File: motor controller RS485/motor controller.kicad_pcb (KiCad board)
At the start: 2 copper layers, 38 x 18 mm, 29 parts, among them IC1 MA702, IC2 MC33926PNB, IC3 LP38690SD-ADJ_NOPB, IC4 LTC2850IS8PBF, J1 Conn_01x04_Male, J2 Conn_01x04_Male, J3 Conn_01x04_Male, M1 Motor_DC, U1 STM32L432KCUx, Y1 32mhz

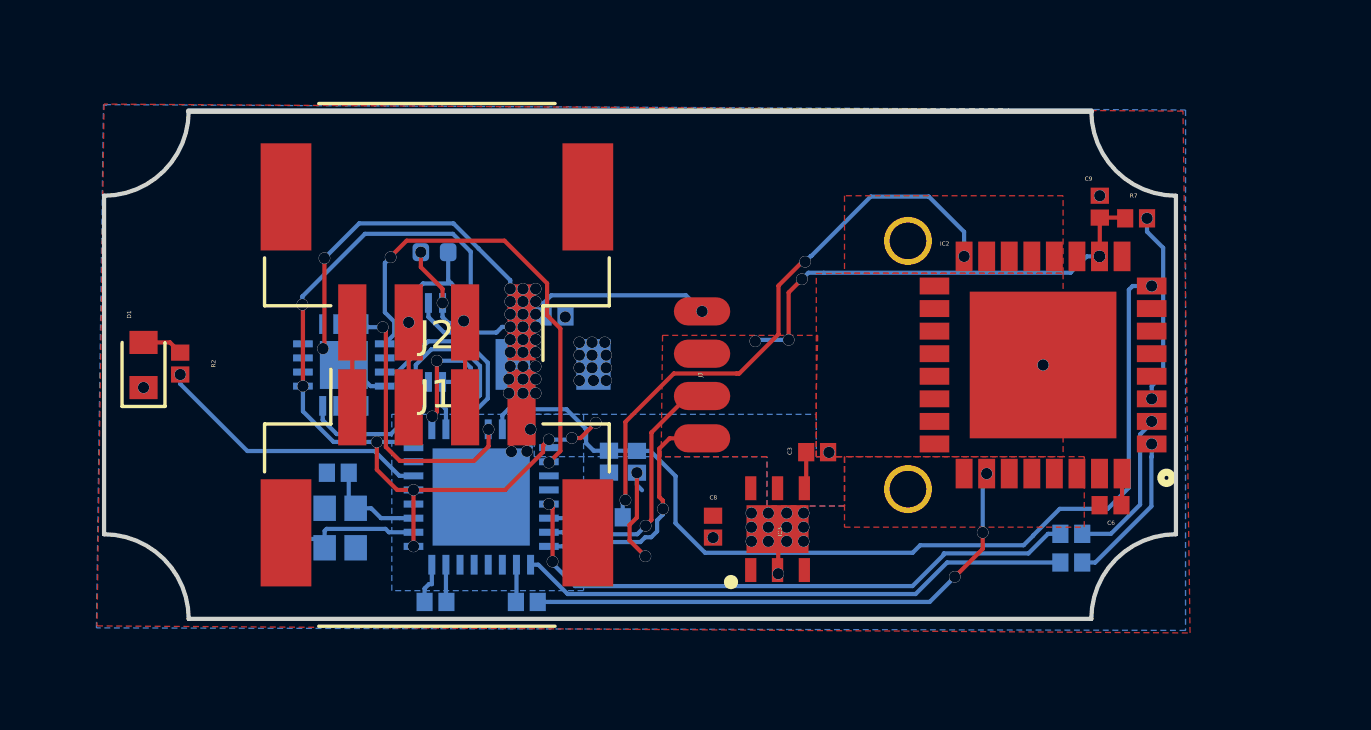
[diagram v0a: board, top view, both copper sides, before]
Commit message: Updated RS485 variant
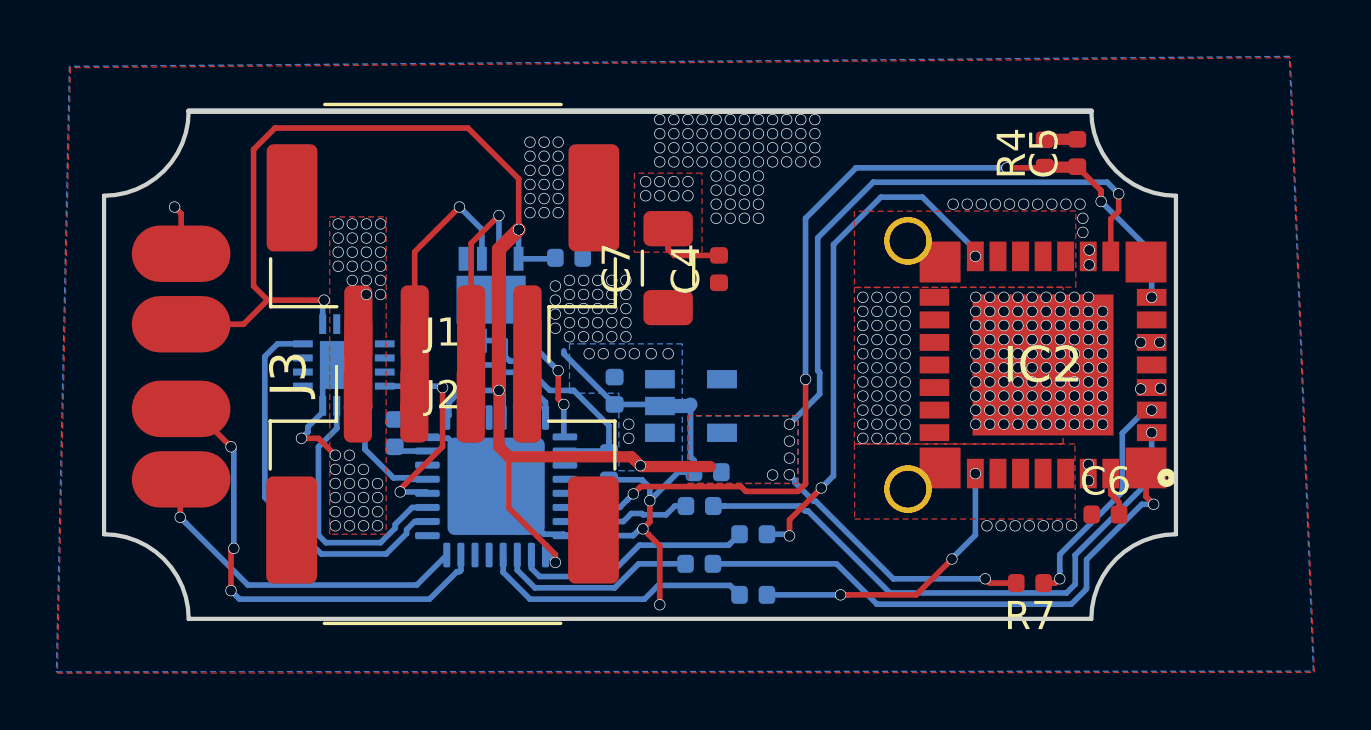
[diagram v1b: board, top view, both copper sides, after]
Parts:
- removed C8, C9: 1UF, Capacitor_SMD:C_0402_1005Metric
- removed D1: LED, LED_SMD:LED_0603_1608Metric
- removed IC4: LTC2850IS8PBF, SOIC127P600X175-8N
- removed R2: 330, Resistor_SMD:R_0402_1005Metric
- removed Y1: 32mhz, Crystal:Crystal_SMD_2016-4Pin_2.0x1.6mm
- added U2: MIC5504-3.3YM5, Package_TO_SOT_SMD:SOT-23-5, B.Cu at (20.8, 10.5)
- C1, C2: value 10pF -> C
- C3: moved to B.Cu
- C4, C5, C7, R4: moved to F.Cu
- IC2: footprint MC33926PNB:QFN80P800X800X220-33N -> MC33926:QFN80P800X800X220-33N
- IC3: value LP38690SD-ADJ_NOPB -> SN65HVD75DRBT; footprint LP38690SD-ADJ_NOPB:SON95P300X300X80-7N -> SN65HVD75DRBT:SON65P300X300X100-9N-D; moved to B.Cu
- R3: value 120 -> 10K
- moved C5 19.9 mm to (34.5, 1.49), turned to 90 degrees
- moved J3 18.5 mm to (2.73, 9.06)
- moved R4 18.1 mm to (33.4, 1.50), turned to 90 degrees
- moved R7 13.5 mm to (32.8, 16.7)
- moved R6 13.2 mm to (21.1, 14.0)
- moved R5 13.2 mm to (21.1, 16.1)
- moved IC3 13.0 mm to (13.7, 6.69)
- moved C1 12.6 mm to (18.1, 9.91)
- moved C2 11.2 mm to (16.5, 5.20), turned to 180 degrees
- moved R3 9.79 mm to (17.9, 12.6), turned to 90 degrees
- moved R8 8.03 mm to (23.0, 17.1)
- moved J2 7.98 mm to (12.0, 5.02), turned to 180 degrees
- moved J1 7.91 mm to (12.0, 12.9), turned to 0 degrees
- moved R1 6.16 mm to (10.3, 11.4), turned to 90 degrees
- moved C4 6.07 mm to (21.8, 5.60), turned to 90 degrees
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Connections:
- C1 pad 1: Net-(C1-Pad1) -> GND
- C1 pad 2: GND -> +BATT
- C2 pad 2: Net-(C2-Pad2) -> +3V3
- IC3 pad 1: +BATT -> RX
- IC3 pad 2: GND -> DIR
- IC3 pad 3: Net-(IC3-Pad3) -> DIR
- IC3 pad 4: +3V3 -> TX
- IC3 pad 5: +3V3 -> GND
- IC3 pad 6: +BATT -> A
- IC3 pad 7: GND -> B
- J2 pad MP: (no net) -> +BATT
- R3 pad 1: B -> GND
- R3 pad 2: A -> DIR
- U1 pad 11: SCK -> Net-(U1-Pad11)
- U1 pad 12: MISO -> Net-(U1-Pad12)
- U1 pad 13: MOSI -> Net-(U1-Pad13)
- U1 pad 15: Net-(U1-Pad15) -> IN1
- U1 pad 18: ENC_CS -> D2
- U1 pad 19: Net-(U1-Pad19) -> IN2
- U1 pad 2: Net-(C1-Pad1) -> Net-(U1-Pad2)
- U1 pad 20: Net-(U1-Pad20) -> D1
- U1 pad 21: IN1 -> Net-(U1-Pad21)
- U1 pad 22: D2 -> Net-(U1-Pad22)
- U1 pad 25: IN2 -> Net-(U1-Pad25)
- U1 pad 26: D1 -> SCK
- U1 pad 27: Net-(U1-Pad27) -> MISO
- U1 pad 28: Net-(U1-Pad28) -> MOSI
- U1 pad 29: Net-(U1-Pad29) -> ENC_CS
- U1 pad 3: Net-(C2-Pad2) -> Net-(U1-Pad3)
- U1 pad 6: signaling -> Net-(U1-Pad6)
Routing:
- net +3V3: track 47.2 -> 81.4 mm
- net IN1: track 21.3 -> 4.56 mm, vias 2 -> 0
- net Net-(IC2-Pad2): track 5.60 -> 20.7 mm
- net Net-(IC2-Pad1): track 5.49 -> 19.7 mm
- net IN2: track 19.7 -> 7.11 mm
- net ENC_CS: track 16.6 -> 4.19 mm, vias 2 -> 0
- net signaling: track 9.95 -> 0.00 mm, vias 1 -> 0
- net Net-(IC2-Pad26): track 19.3 -> 10.5 mm
- net D1: track 1.33 -> 9.72 mm
- net SWDIO: track 9.30 -> 16.7 mm, vias 1 -> 3
- net D2: track 1.85 -> 8.59 mm
- net DIR: track 2.25 -> 8.62 mm
- net Net-(C1-Pad1): track 5.27 -> 0.00 mm
- net Net-(C2-Pad2): track 3.56 -> 0.00 mm
- net SWCLK: track 8.80 -> 12.2 mm
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- added copper zone on B.Cu, net +BATT
- added copper zone on In1.Cu, net +BATT
- added copper zone on In2.Cu, net GND
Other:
- copper layers 2 -> 4
- net class Default: clearance 0.127 -> 0.2; trace_width 0.15 -> 0.2; via_dia 0.41 -> 0.4; via_drill 0.4 -> 0.35
- rule trace_clearance: 0.127 -> 0.2
- rule trace_min: 0.127 -> 0.2
